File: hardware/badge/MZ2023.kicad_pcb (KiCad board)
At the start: 2 copper layers, 77 x 51.4 mm, 88 parts, among them J1 Conn_01x04, J2 Conn_01x04, J3 Conn_01x04, J4 Conn_01x04, J5 Conn_01x10_Female, J6 Conn_01x02_Male, J7 Conn_01x05_Female, J8 Conn_Coaxial, J9 Conn_02x03_Counter_Clockwise, Q2 DMG2301L, SW1 SW_Push, SW3 SW_Push, SW4 SW_Push_SPDT, U1 Pico, U2 LoRa-E5, U3 MCP73831-2-OT

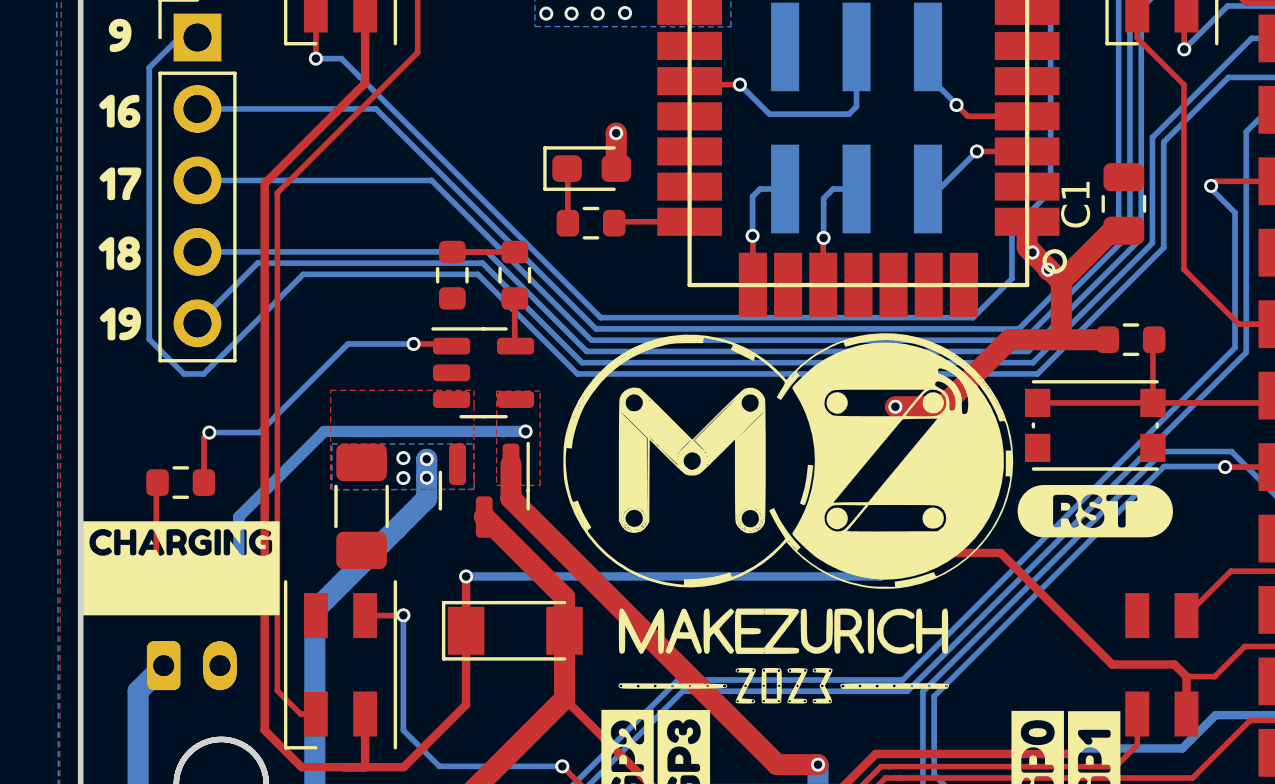
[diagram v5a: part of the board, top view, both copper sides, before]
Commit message: changing silk: lipo charge LED -> CHG
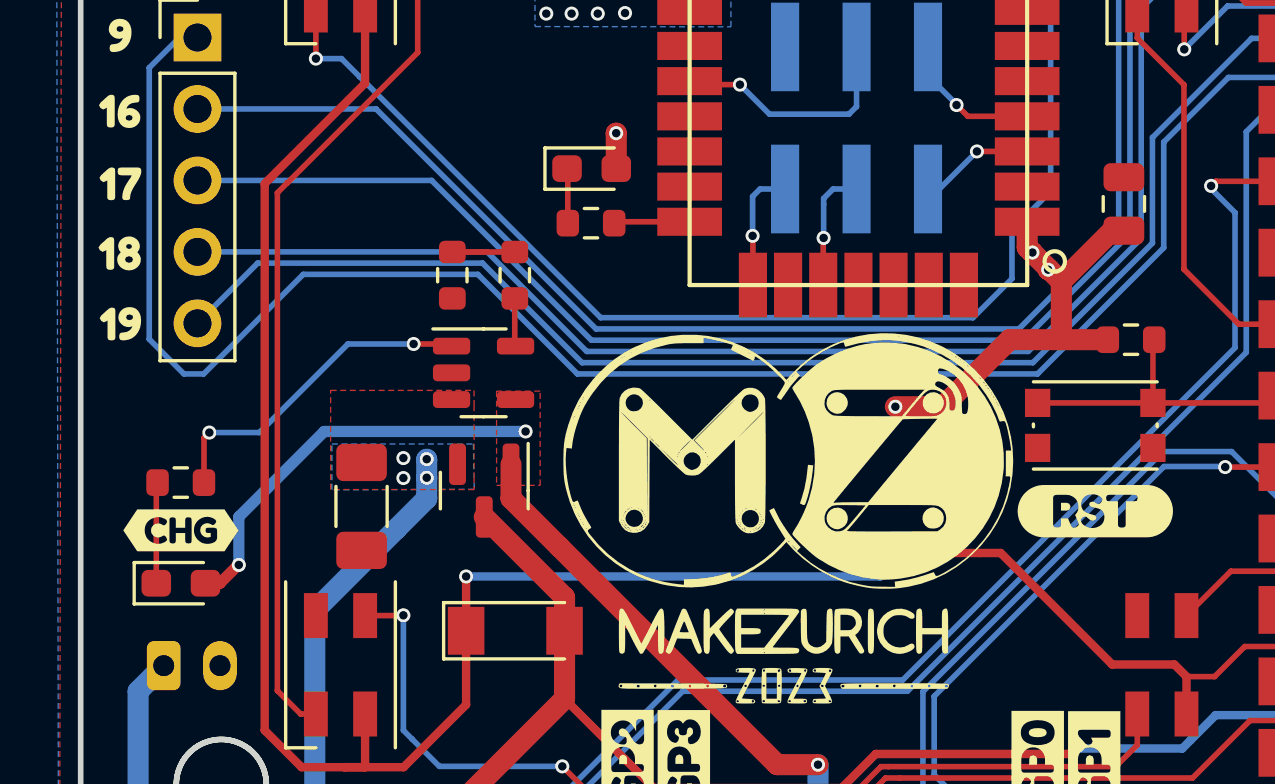
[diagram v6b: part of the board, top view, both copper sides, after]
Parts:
- removed kibuzzard-645D57F9: G***, kibuzzard-645D57F9
- added kibuzzard-6461287C: G***, kibuzzard-6461287C, F.Cu at (101.3, 101.5)
